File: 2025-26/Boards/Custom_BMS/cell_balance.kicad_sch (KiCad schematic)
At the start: 27 parts

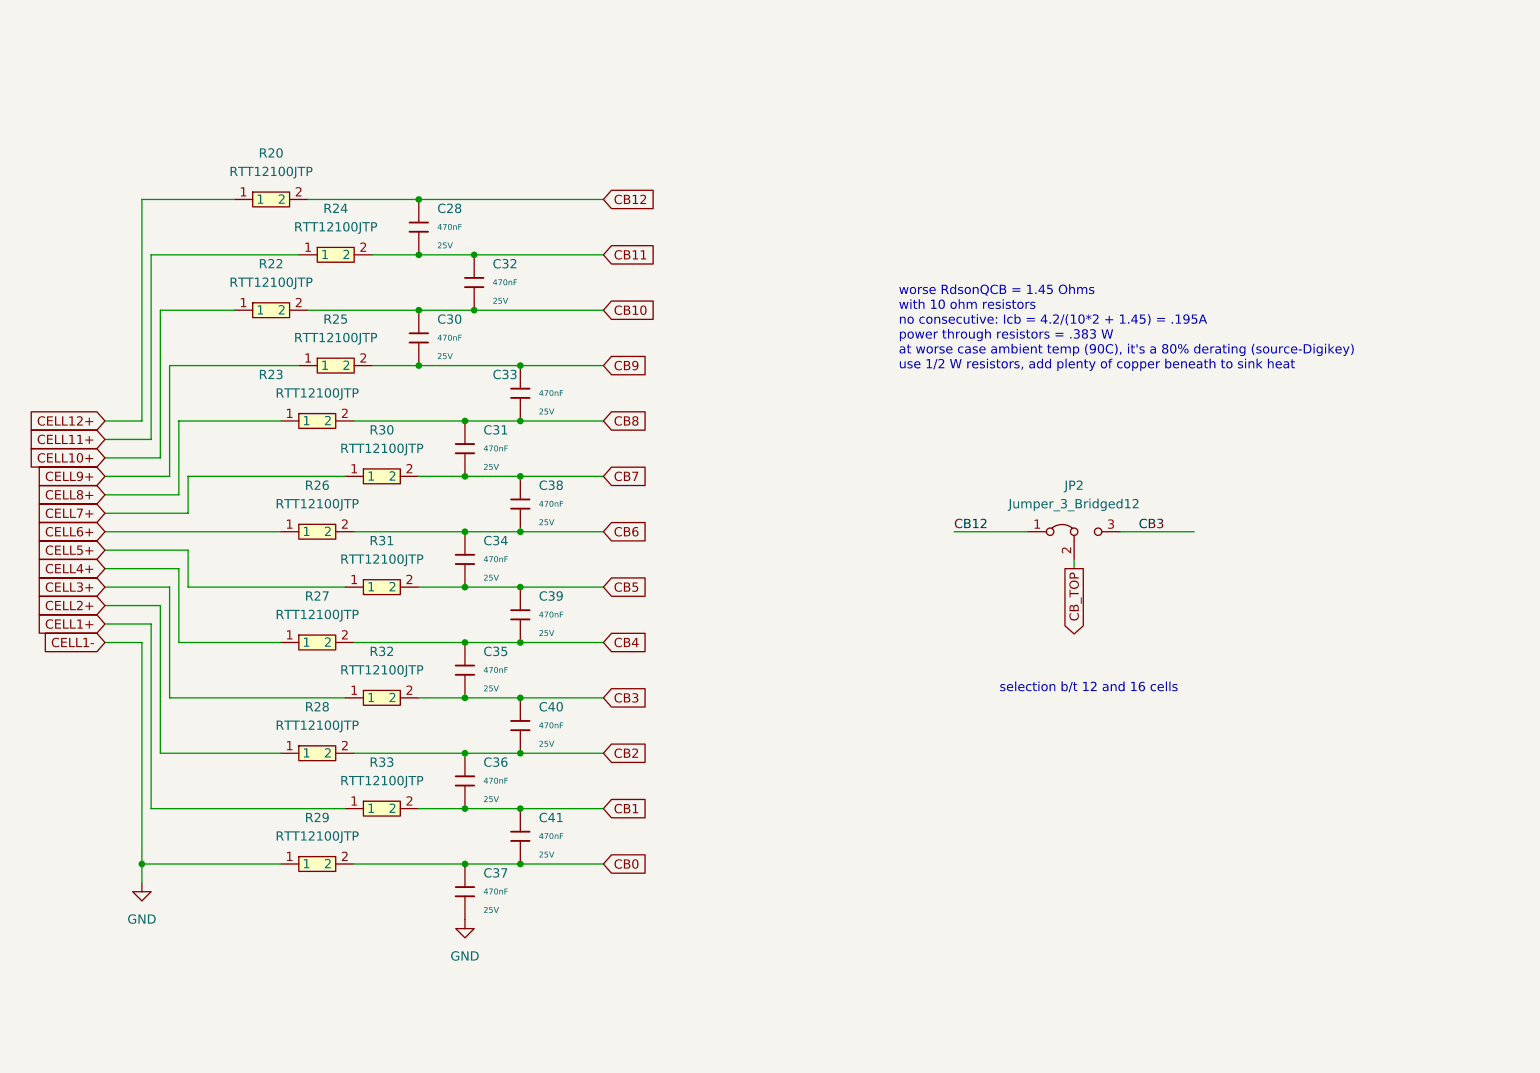
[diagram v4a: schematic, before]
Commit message: fixed some layout and schematic issues
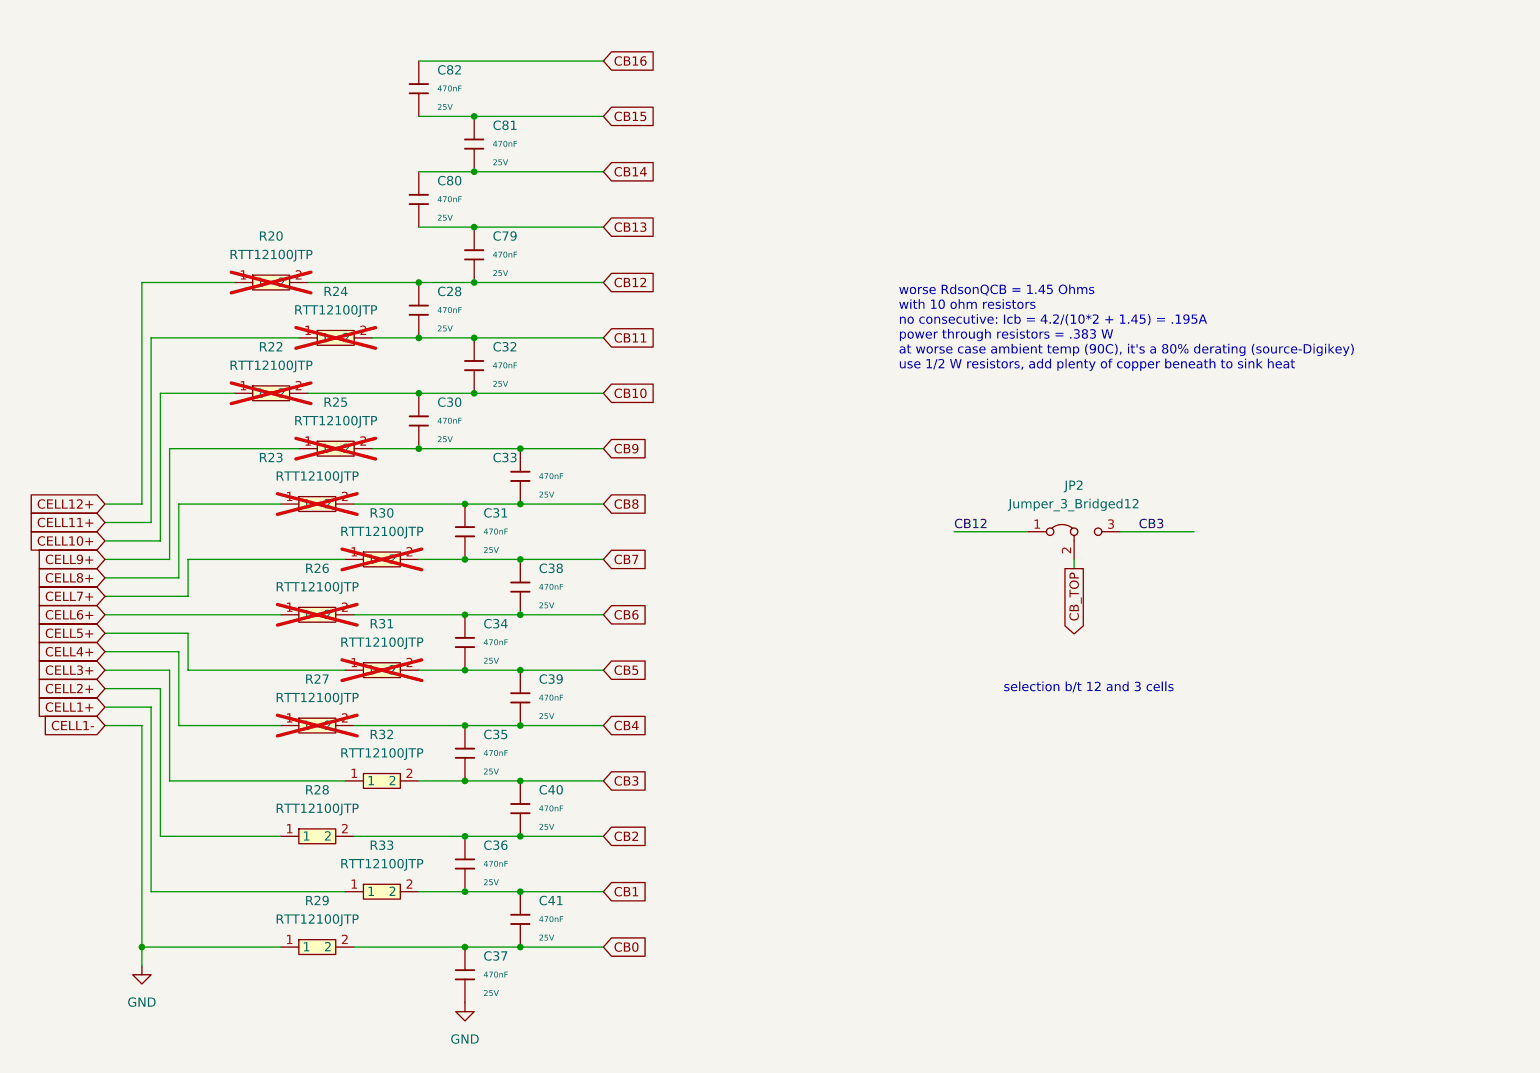
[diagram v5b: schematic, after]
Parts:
- added C79, C80, C81, C82: 470nF, PCM_JLCPCB:C_0603, symbol PCM_JLCPCB-Capacitors:0603,470nF
- R20, R22, R23, R24, R25, R26, R27, R30, R31: now not fitted; now left out of the parts list
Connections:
- net CB12: now also C79.2
- new net CB13: C79.1, C80.2
- new net CB14: C80.1, C81.2
- new net CB15: C81.1, C82.2
- new net CB16: C82.1
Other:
- note added: "selection b/t 12 and 3 cells"
- note removed: "selection b/t 12 and 16 cells"
- moved on the sheet: C28, C30, C31, C32, C33, C34, C35, C36, C37, C38, C39, C40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

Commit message: fixed review items
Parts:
- R27: now fitted; now in the parts list
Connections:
- net CB3: no longer JP2.3 (B)
- net CB4: now also JP2.3 (B)
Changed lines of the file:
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@@
 		)
 	)
-	(label "CB3"
+	(label "CB4"
 		(at 201.93 104.14 0)
 		(effects
@@
 		(unit 1)
 		(exclude_from_sim no)
-		(in_bom no)
+		(in_bom yes)
 		(on_board yes)
-		(dnp yes)
+		(dnp no)
 		(fields_autoplaced yes)
 		(property "Reference" "R27"

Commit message: final fixes ??
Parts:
- removed JP2: Jumper_3_Bridged12, Connector_PinHeader_2.00mm:PinHeader_1x03_P2.00mm_Vertical, symbol Jumper:Jumper_3_Bridged12
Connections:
- net GND: no longer R29.1
- new net CELL1-: R29.1
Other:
- note removed: "selection b/t 12 and 3 cells"
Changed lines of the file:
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@@
 		)
 	)
-	(text "selection b/t 12 and 3 cells"
-		(exclude_from_sim no)
-		(at 195.072 125.73 0)
-		(effects
-			(font
-				(size 1.27 1.27)
-			)
-		)
-	)
 	(junction
 		(at 109.22 138.43)
@@
 	)
 	(junction
-		(at 64.77 161.29)
-		(diameter 0)
-		(color 0 0 0 0)
-	)
-	(junction
 		(at 109.22 146.05)
 		(diameter 0)
@@
 	(wire
 		(pts
-			(xy 176.53 104.14) (xy 186.69 104.14)
-		)
-		(stroke
-			(width 0)
-			(type default)
-		)
-	)
-	(wire
-		(pts
 			(xy 69.85 120.65) (xy 69.85 130.81)
 		)
@@
 	(wire
 		(pts
-			(xy 64.77 161.29) (xy 64.77 163.83)
-		)
-		(stroke
-			(width 0)
-			(type default)
-		)
-	)
-	(wire
-		(pts
 			(xy 59.69 123.19) (xy 68.58 123.19)
 		)
@@
 	(wire
 		(pts
-			(xy 193.04 107.95) (xy 193.04 109.22)
-		)
-		(stroke
-			(width 0)
-			(type default)
-		)
-	)
-	(wire
-		(pts
 			(xy 102.87 54.61) (xy 110.49 54.61)
 		)
@@
 	(wire
 		(pts
-			(xy 199.39 104.14) (xy 209.55 104.14)
-		)
-		(stroke
-			(width 0)
-			(type default)
-		)
-	)
-	(wire
-		(pts
 			(xy 116.84 107.95) (xy 128.27 107.95)
 		)
@@
 		)
 	)
-	(label "CB4"
-		(at 201.93 104.14 0)
-		(effects
-			(font
-				(size 1.27 1.27)
-			)
-			(justify left bottom)
-		)
-	)
-	(label "CB12"
-		(at 176.53 104.14 0)
-		(effects
-			(font
-				(size 1.27 1.27)
-			)
-			(justify left bottom)
-		)
-	)
-	(global_label "CB_TOP"
-		(shape output)
-		(at 193.04 109.22 270)
-		(fields_autoplaced yes)
-		(effects
-			(font
-				(size 1.27 1.27)
-			)
-			(justify right)
-		)
-		(property "Intersheetrefs" "${INTERSHEET_REFS}"
-			(at 193.04 119.2809 90)
-			(effects
-				(font
-					(size 1.27 1.27)
-				)
-				(justify right)
-				(hide yes)
-			)
-		)
-	)
 	(global_label "CELL9+"
 		(shape input)
@@
 	)
 	(symbol
-		(lib_id "power:GND")
-		(at 64.77 163.83 0)
-		(unit 1)
-		(exclude_from_sim no)
-		(in_bom yes)
-		(on_board yes)
-		(dnp no)
-		(fields_autoplaced yes)
-		(property "Reference" "#PWR060"
-			(at 64.77 170.18 0)
-			(effects
-				(font
-					(size 1.27 1.27)
-				)
-				(hide yes)
-			)
-		)
-		(property "Value" "GND"
-			(at 64.77 168.91 0)
-			(effects
-				(font
-					(size 1.27 1.27)
-				)
-			)
-		)
-		(property "Footprint" ""
-			(at 64.77 163.83 0)
-			(effects
-				(font
-					(size 1.27 1.27)
-				)
-				(hide yes)
-			)
-		)
-		(property "Datasheet" ""
-			(at 64.77 163.83 0)
-			(effects
-				(font
-					(size 1.27 1.27)
-				)
-				(hide yes)
-			)
-		)
-		(property "Description" "Power symbol creates a global label with name \"GND\" , ground"
-			(at 64.77 163.83 0)
-			(effects
-				(font
-					(size 1.27 1.27)
-				)
-				(hide yes)
-			)
-		)
-		(pin "1"
-		)
-		(instances
-			(project "Custom_BMS"
-				(path "/570d6d9c-ebf5-4f83-96f6-d3309a3e637d/e94a219a-300a-4436-8821-3bf884f472d1"
-					(reference "#PWR060")
-					(unit 1)
-				)
-			)
-		)
-	)
-	(symbol
 		(lib_id "easyeda2kicad:RTT12100JTP")
 		(at 88.9 115.57 0)
@@
 	)
 	(symbol
-		(lib_id "Jumper:Jumper_3_Bridged12")
-		(at 193.04 104.14 0)
-		(unit 1)
-		(exclude_from_sim no)
-		(in_bom no)
-		(on_board yes)
-		(dnp no)
-		(fields_autoplaced yes)
-		(property "Reference" "JP2"
-			(at 193.04 97.79 0)
-			(effects
-				(font
-					(size 1.27 1.27)
-				)
-			)
-		)
-		(property "Value" "Jumper_3_Bridged12"
-			(at 193.04 100.33 0)
-			(effects
-				(font
-					(size 1.27 1.27)
-				)
-			)
-		)
-		(property "Footprint" "Connector_PinHeader_2.00mm:PinHeader_1x03_P2.00mm_Vertical"
-			(at 193.04 104.14 0)
-			(effects
-				(font
-					(size 1.27 1.27)
-				)
-				(hide yes)
-			)
-		)
-		(property "Datasheet" "~"
-			(at 193.04 104.14 0)
-			(effects
-				(font
-					(size 1.27 1.27)
-				)
-				(hide yes)
-			)
-		)
-		(property "Description" "Jumper, 3-pole, pins 1+2 closed/bridged"
-			(at 193.04 104.14 0)
-			(effects
-				(font
-					(size 1.27 1.27)
-				)
-				(hide yes)
-			)
-		)
-		(pin "2"
-		)
-		(pin "3"
-		)
-		(pin "1"
-		)
-		(instances
-			(project "Custom_BMS"
-				(path "/570d6d9c-ebf5-4f83-96f6-d3309a3e637d/e94a219a-300a-4436-8821-3bf884f472d1"
-					(reference "JP2")
-					(unit 1)
-				)
-			)
-		)
-	)
-	(symbol
 		(lib_id "easyeda2kicad:RTT12100JTP")
 		(at 82.55 85.09 0)
@@
 		(on_board yes)
 		(dnp no)
-		(fields_autoplaced yes)
 		(property "Reference" "#PWR04"
 			(at 109.22 175.26 0)
@@
 		)
 		(property "Value" "GND"
-			(at 109.22 173.99 0)
+			(at 109.22 172.974 0)
 			(effects
 				(font
